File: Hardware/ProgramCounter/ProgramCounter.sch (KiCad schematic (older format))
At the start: 4 parts

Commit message: Started to make Schematic for the Program Counter.
TODO: Complete schematic, buy parts, layout PCB, solder PCB.

Then logically test the PCB using a digital oscilloscope.

Then repeat for 4-5 other PCBs.
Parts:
- removed UNOT: 74AUC1G04, symbol 74xGxx:74AUC1G04
- added C1, C2, C3, C4, C5, C6, C7: .1uF, symbol Device:C
- added U1: 74LS684, Package_SO:SSOP-20_3.9x8.7mm_P0.635mm, symbol 74xx_IEEE:74LS684
- added U2: 74151, Package_SO:SOP-16_4.55x10.3mm_P1.27mm, symbol 74xx_IEEE:74151
- added UNAND1: 74LS00, Package_SO:TSSOP-14_4.4x5mm_P0.65mm, symbol 74xx:74LS00
- added UQAND1: 74LS21, Package_SO:MSOP-12-16_3x4mm_P0.5mm, symbol 74xx:74LS21
- added UXOR1: 74HC86, Package_SO:SOIC-14_3.9x8.7mm_P1.27mm, symbol 74xx:74HC86
- J1: renamed from J?; footprint (none) -> Connector_PinSocket_2.54mm:PinSocket_2x32_P2.54mm_Horizontal
- UPR0, UPR1: footprint (none) -> Package_SO:SOIC-20W_7.5x12.8mm_P1.27mm
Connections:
- net labels added: IMM0, IMM1, IMM2, IMM3, IMM[0..3], IS_JMP, IS_SKIP, OPCODE[0..3], PCINC[0..15], PCOUT[0..15], RCD0, RCD1, RCD2, RCD3, RCD4, RCD5, RCD6, RCD7, RCD[0..3], RCS0, RCS1, RCS2, RCS3, RCS4, RCS5, RCS6, RCS7, RCS[0..3], REGMEM[0..15], cmpeq, cmpgt, cmplt
- net labels removed: OPCODE, PCINC, PCOUT, REGMEM
- wire segments 82 -> 183
- no-connect marks 1 -> 7
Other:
- note added: "Choose which condition to skip/jump on"
- moved on the sheet: UPR0, UPR1

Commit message: PC PCB Progress
Mostly done with schematic for the Program Counter. I'll order parts soon and start on the PCB design next. It'll be my first four layer board!

Based on what I've seen so far, CMOS seems to be more prevalent than TTL, so I'll make this computer out of CMOS.
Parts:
- removed J1: Conn_02x32_Row_Letter_First, Connector_PinSocket_2.54mm:PinSocket_2x32_P2.54mm_Horizontal, symbol Connector_Generic:Conn_02x32_Row_Letter_First
- added J1, J2: Conn_02x16_Counter_Clockwise, Connector_PinHeader_2.54mm:PinHeader_2x16_P2.54mm_Horizontal, symbol Connector_Generic:Conn_02x16_Counter_Clockwise
- added TP?: TP_PCEVENT, symbol Connector:TestPoint
- C1, C2, C3, C4, C5, C6, C7: footprint (none) -> Capacitor_SMD:C_1206_3216Metric_Pad1.42x1.75mm_HandSolder
- UQAND1: footprint Package_SO:MSOP-12-16_3x4mm_P0.5mm -> Package_SO:MSOP-12_3x4mm_P0.65mm
- renumbered U1 to UCMP1, U2 to UCONDMUX1
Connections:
- net labels added: JINST, PCEVENT, SINST, ~IS_JMP, ~IS_SKIP, ~OPCODE0, ~OPCODE1
- net labels removed: IS_JMP
- wire segments 183 -> 186
- no-connect marks 7 -> 4
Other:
- note added: "14ns"
- note added: "55ns"
- note added: "64ns"
- note added: "7ns"
- note added: "8ns"
- note added: "HC21 -> 22ns"
- note added: "HC86 -> 20ns"
- moved on the sheet: C1, C2, C3, C4, C5, C6, C7, UNAND1A, UNAND1B, UNAND1C, UNAND1D, UNAND1E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

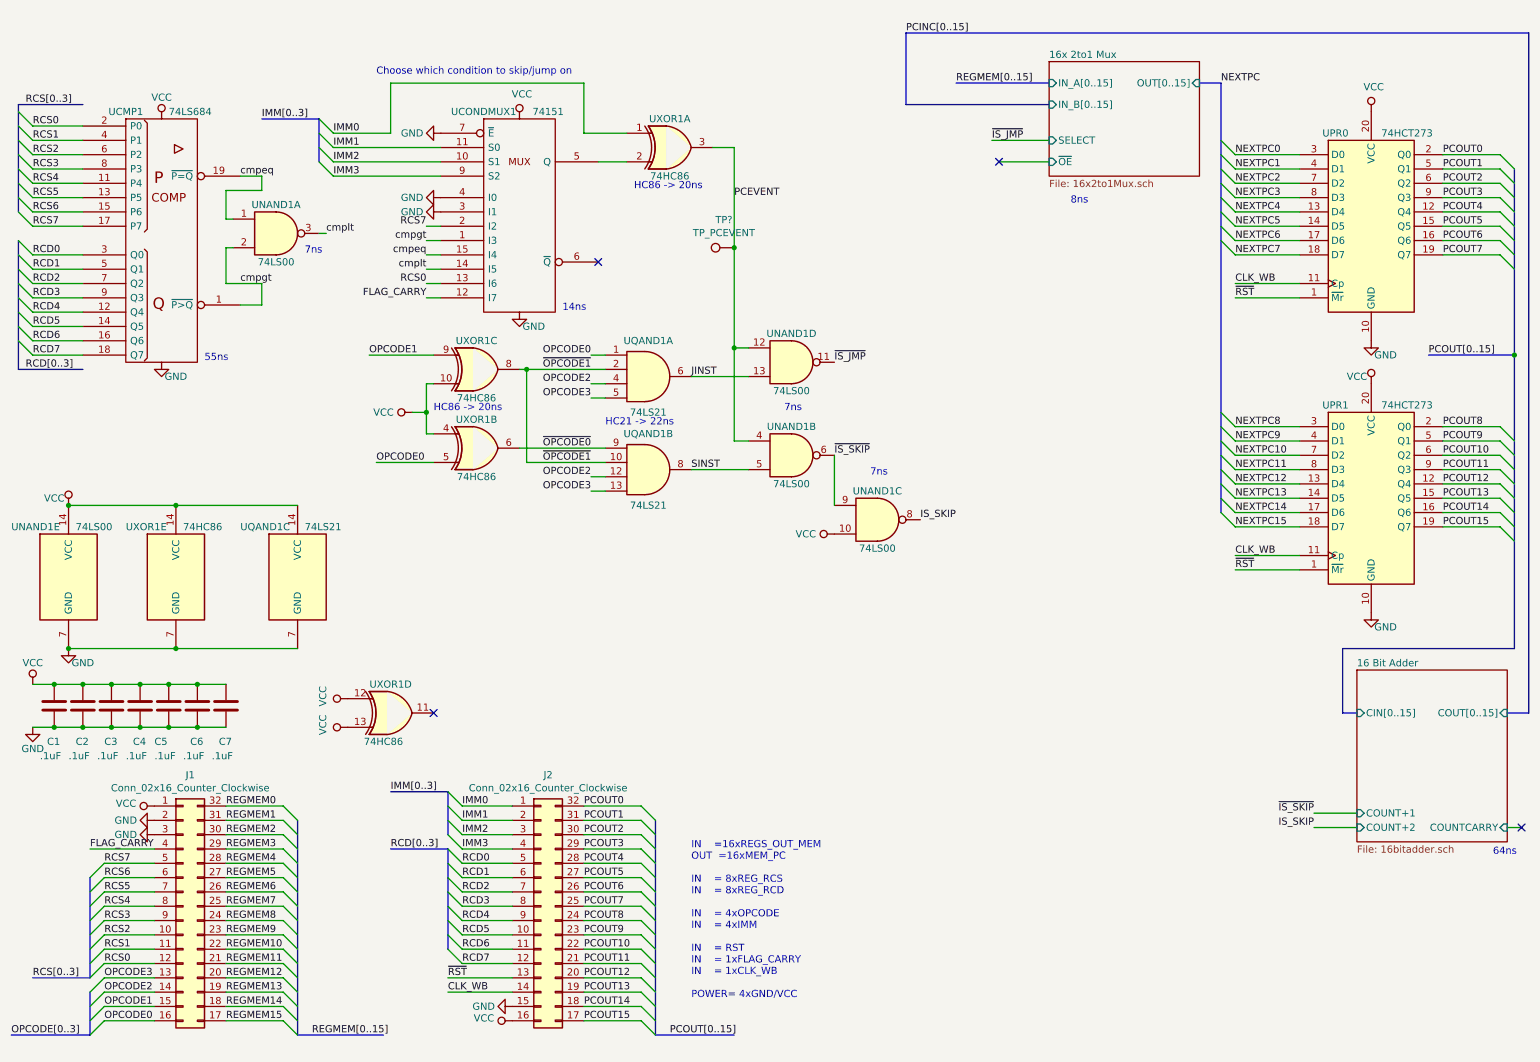
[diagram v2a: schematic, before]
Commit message: PC Schematic
Mostly finished Program Counter schematic. I'm basing the hardware largely off of TI's new HCS family of SN74HCS chips.
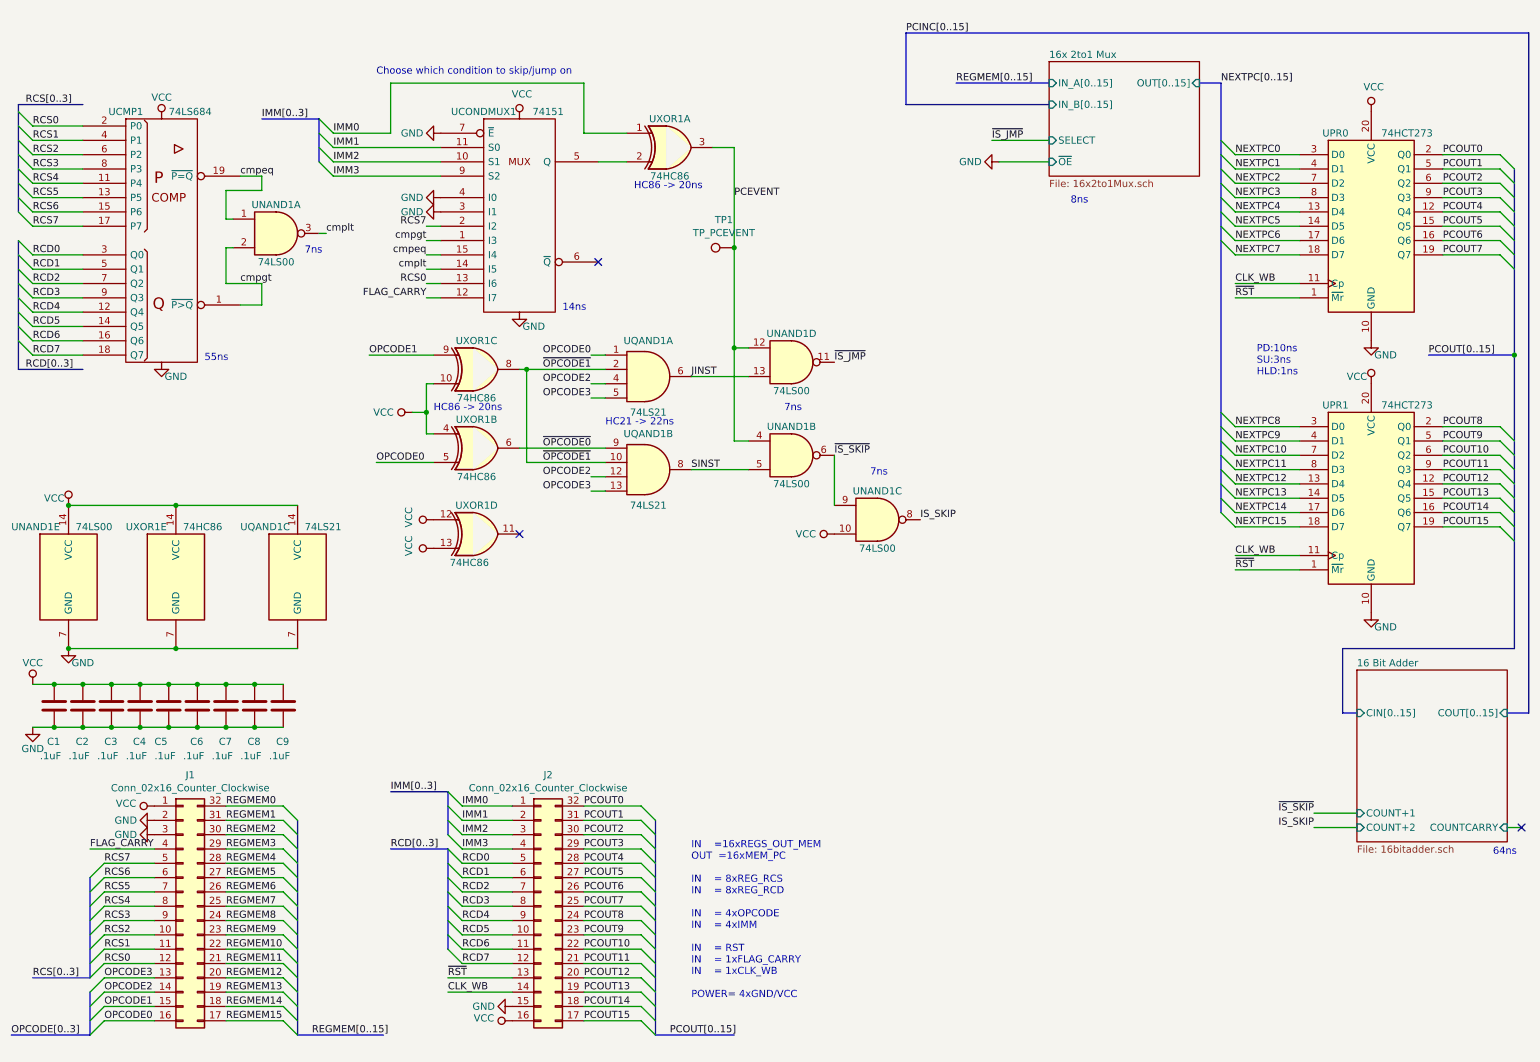
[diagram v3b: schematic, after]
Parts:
- added C8, C9: .1uF, Capacitor_SMD:C_1206_3216Metric_Pad1.42x1.75mm_HandSolder, symbol Device:C
- TP1: renamed from TP?; footprint (none) -> Connector_PinHeader_2.54mm:PinHeader_1x01_P2.54mm_Vertical
- UCMP1: footprint Package_SO:SSOP-20_3.9x8.7mm_P0.635mm -> aFootprint:DW0020A
- UCONDMUX1: footprint Package_SO:SOP-16_4.55x10.3mm_P1.27mm -> aFootprint:R-PDSO-G16
- UNAND1: footprint Package_SO:TSSOP-14_4.4x5mm_P0.65mm -> aFootprint:R-PDSO-G14
- UPR0, UPR1: footprint Package_SO:SOIC-20W_7.5x12.8mm_P1.27mm -> Package_SO:TSSOP-20_4.4x6.5mm_P0.65mm
- UQAND1: footprint Package_SO:MSOP-12_3x4mm_P0.65mm -> aFootprint:R-PDSO-G14
- UXOR1: footprint Package_SO:SOIC-14_3.9x8.7mm_P1.27mm -> aFootprint:R-PDSO-G14
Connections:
- net GND: now also C8.2, C9.2
- net VCC: now also C8.1, C9.1
- no-connect marks 4 -> 3
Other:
- note added: "PD:10ns\nSU:3ns\nHLD:1ns"
- moved on the sheet: UXOR1D
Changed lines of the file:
@@
 F 0 "UPR1" H 9750 4550 50  0000 C CNN
 F 1 "74HCT273" H 10250 4550 50  0000 C CNN
-F 2 "Package_SO:SOIC-20W_7.5x12.8mm_P1.27mm" H 10000 3900 50  0001 C CNN
+F 2 "Package_SO:TSSOP-20_4.4x6.5mm_P0.65mm" H 10000 3900 50  0001 C CNN
 F 3 "https://assets.nexperia.com/documents/data-sheet/74HC_HCT273.pdf" H 10000 3900 50  0001 C CNN
 	1    10000 3900
@@
 F 0 "UPR0" H 9750 2650 50  0000 C CNN
 F 1 "74HCT273" H 10250 2650 50  0000 C CNN
-F 2 "Package_SO:SOIC-20W_7.5x12.8mm_P1.27mm" H 10000 2000 50  0001 C CNN
+F 2 "Package_SO:TSSOP-20_4.4x6.5mm_P0.65mm" H 10000 2000 50  0001 C CNN
 F 3 "https://assets.nexperia.com/documents/data-sheet/74HC_HCT273.pdf" H 10000 2000 50  0001 C CNN
 	1    10000 2000
@@
 	8950 4000 9050 4100
 Text Label 8950 1000 0    50   ~ 0
-NEXTPC
+NEXTPC[0..15]
 Text Label 3550 7350 0    50   ~ 0
 CLK_WB
@@
 Wire Wire Line
 	7750 1550 7400 1550
-NoConn ~ 7400 1550
 Wire Bus Line
 	7100 1000 7750 1000
@@
 F 0 "UCMP1" H 1300 3000 50  0000 C CNN
 F 1 "74LS684" H 1750 3000 50  0000 C CNN
-F 2 "Package_SO:SSOP-20_3.9x8.7mm_P0.635mm" H 1550 2100 50  0001 C CNN
+F 2 "aFootprint:DW0020A" H 1550 2100 50  0001 C CNN
 F 3 "" H 1550 2100 50  0001 C CNN
 	1    1550 2100
@@
 F 0 "UNAND1" H 6550 4250 50  0000 C CNN
 F 1 "74LS00" H 6550 3850 50  0000 C CNN
-F 2 "Package_SO:TSSOP-14_4.4x5mm_P0.65mm" H 6550 4050 50  0001 C CNN
+F 2 "aFootprint:R-PDSO-G14" H 6550 4050 50  0001 C CNN
 F 3 "http://www.ti.com/lit/gpn/sn74ls00" H 6550 4050 50  0001 C CNN
 	3    6550 4050
@@
 F 0 "UNAND1" H 5950 3150 50  0000 C CNN
 F 1 "74LS00" H 5950 2750 50  0000 C CNN
-F 2 "Package_SO:TSSOP-14_4.4x5mm_P0.65mm" H 5950 2950 50  0001 C CNN
+F 2 "aFootprint:R-PDSO-G14" H 5950 2950 50  0001 C CNN
 F 3 "http://www.ti.com/lit/gpn/sn74ls00" H 5950 2950 50  0001 C CNN
 	4    5950 2950
@@
 F 0 "UNAND1" H 500 4800 50  0000 L CNN
 F 1 "74LS00" H 950 4800 50  0000 L CNN
-F 2 "Package_SO:TSSOP-14_4.4x5mm_P0.65mm" H 900 4450 50  0001 C CNN
+F 2 "aFootprint:R-PDSO-G14" H 900 4450 50  0001 C CNN
 F 3 "http://www.ti.com/lit/gpn/sn74ls00" H 900 4450 50  0001 C CNN
 	5    900  4450
@@
 F 0 "UCONDMUX1" H 3800 2600 50  0000 C CNN
 F 1 "74151" H 4250 2600 50  0000 C CNN
-F 2 "Package_SO:SOP-16_4.55x10.3mm_P1.27mm" H 4050 1900 50  0001 C CNN
+F 2 "aFootprint:R-PDSO-G16" H 4050 1900 50  0001 C CNN
 F 3 "" H 4050 1900 50  0001 C CNN
 	1    4050 1900
@@
 L 74xx:74HC86 UXOR1
 U 4 1 62FEDD88
-P 3150 5400
-F 0 "UXOR1" H 3150 5600 50  0000 C CNN
-F 1 "74HC86" H 3100 5200 50  0000 C CNN
-F 2 "Package_SO:SOIC-14_3.9x8.7mm_P1.27mm" H 3150 5400 50  0001 C CNN
-F 3 "http://www.ti.com/lit/gpn/sn74HC86" H 3150 5400 50  0001 C CNN
-	4    3150 5400
+P 3750 4150
+F 0 "UXOR1" H 3750 4350 50  0000 C CNN
+F 1 "74HC86" H 3700 3950 50  0000 C CNN
+F 2 "aFootprint:R-PDSO-G14" H 3750 4150 50  0001 C CNN
+F 3 "http://www.ti.com/lit/gpn/sn74HC86" H 3750 4150 50  0001 C CNN
+	4    3750 4150
 	1    0    0    -1
 $EndComp
@@
 F 0 "UXOR1" H 1300 4800 50  0000 L CNN
 F 1 "74HC86" H 1700 4800 50  0000 L CNN
-F 2 "Package_SO:SOIC-14_3.9x8.7mm_P1.27mm" H 1650 4450 50  0001 C CNN
+F 2 "aFootprint:R-PDSO-G14" H 1650 4450 50  0001 C CNN
 F 3 "http://www.ti.com/lit/gpn/sn74HC86" H 1650 4450 50  0001 C CNN
 	5    1650 4450
@@
 F 0 "UQAND1" H 4950 3950 50  0000 C CNN
 F 1 "74LS21" H 4950 3450 50  0000 C CNN
-F 2 "Package_SO:MSOP-12_3x4mm_P0.65mm" H 4950 3700 50  0001 C CNN
+F 2 "aFootprint:R-PDSO-G14" H 4950 3700 50  0001 C CNN
 F 3 "http://www.ti.com/lit/gpn/sn74LS21" H 4950 3700 50  0001 C CNN
 	2    4950 3700
@@
 F 0 "UXOR1" H 5100 1650 50  0000 C CNN
 F 1 "74HC86" H 5100 1250 50  0000 C CNN
-F 2 "Package_SO:SOIC-14_3.9x8.7mm_P1.27mm" H 5100 1450 50  0001 C CNN
+F 2 "aFootprint:R-PDSO-G14" H 5100 1450 50  0001 C CNN
 F 3 "http://www.ti.com/lit/gpn/sn74HC86" H 5100 1450 50  0001 C CNN
 	1    5100 1450
@@
 F 0 "UQAND1" H 4950 3300 50  0000 C CNN
 F 1 "74LS21" H 4950 2800 50  0000 C CNN
-F 2 "Package_SO:MSOP-12_3x4mm_P0.65mm" H 4950 3050 50  0001 C CNN
+F 2 "aFootprint:R-PDSO-G14" H 4950 3050 50  0001 C CNN
 F 3 "http://www.ti.com/lit/gpn/sn74LS21" H 4950 3050 50  0001 C CNN
 	1    4950 3050
@@
 F 0 "UNAND1" H 2350 2250 50  0000 C CNN
 F 1 "74LS00" H 2350 1850 50  0000 C CNN
-F 2 "Package_SO:TSSOP-14_4.4x5mm_P0.65mm" H 2350 2050 50  0001 C CNN
+F 2 "aFootprint:R-PDSO-G14" H 2350 2050 50  0001 C CNN
 F 3 "http://www.ti.com/lit/gpn/sn74ls00" H 2350 2050 50  0001 C CNN
 	1    2350 2050
@@
 F 0 "UNAND1" H 5950 3800 50  0000 C CNN
 F 1 "74LS00" H 5950 3400 50  0000 C CNN
-F 2 "Package_SO:TSSOP-14_4.4x5mm_P0.65mm" H 5950 3600 50  0001 C CNN
+F 2 "aFootprint:R-PDSO-G14" H 5950 3600 50  0001 C CNN
 F 3 "http://www.ti.com/lit/gpn/sn74ls00" H 5950 3600 50  0001 C CNN
 	2    5950 3600
@@
 	4050 3550 4650 3550
 $Comp
-L power:VCC #PWR?
+L power:VCC #PWR0109
 U 1 1 62FBF0AA
 P 3300 3300
-F 0 "#PWR?" H 3300 3150 50  0001 C CNN
+F 0 "#PWR0109" H 3300 3150 50  0001 C CNN
 F 1 "VCC" V 3300 3500 50  0000 C CNN
 F 2 "" H 3300 3300 50  0001 C CNN
@@
 F 0 "UQAND1" H 2100 4800 50  0000 L CNN
 F 1 "74LS21" H 2550 4800 50  0000 L CNN
-F 2 "Package_SO:MSOP-12_3x4mm_P0.65mm" H 2500 4450 50  0001 C CNN
+F 2 "aFootprint:R-PDSO-G14" H 2500 4450 50  0001 C CNN
 F 3 "http://www.ti.com/lit/gpn/sn74LS21" H 2500 4450 50  0001 C CNN
 	3    2500 4450
@@
 $EndComp
 $Comp
-L power:VCC #PWR?
+L power:VCC #PWR0110
 U 1 1 63082810
 P 650 5200
-F 0 "#PWR?" H 650 5050 50  0001 C CNN
+F 0 "#PWR0110" H 650 5050 50  0001 C CNN
 F 1 "VCC" H 650 5350 50  0000 C CNN
 F 2 "" H 650 5200 50  0001 C CNN
@@
 	650  5200 800  5200
 $Comp
-L power:GND #PWR?
+L power:GND #PWR0136
 U 1 1 63182DD6
 P 650 5500
-F 0 "#PWR?" H 650 5250 50  0001 C CNN
+F 0 "#PWR0136" H 650 5250 50  0001 C CNN
 F 1 "GND" H 650 5350 50  0000 C CNN
 F 2 "" H 650 5500 50  0001 C CNN
@@
 Connection ~ 5550 2850
 $Comp
-L power:VCC #PWR?
+L power:VCC #PWR0137
 U 1 1 6326BAED
-P 2850 5300
-F 0 "#PWR?" H 2850 5150 50  0001 C CNN
-F 1 "VCC" H 2867 5473 50  0000 C CNN
-F 2 "" H 2850 5300 50  0001 C CNN
-F 3 "" H 2850 5300 50  0001 C CNN
-	1    2850 5300
+P 3450 4050
+F 0 "#PWR0137" H 3450 3900 50  0001 C CNN
+F 1 "VCC" H 3467 4223 50  0000 C CNN
+F 2 "" H 3450 4050 50  0001 C CNN
+F 3 "" H 3450 4050 50  0001 C CNN
+	1    3450 4050
 	0    -1   -1   0
 $EndComp
 $Comp
-L power:VCC #PWR?
+L power:VCC #PWR0138
 U 1 1 6326C2DD
-P 2850 5500
-F 0 "#PWR?" H 2850 5350 50  0001 C CNN
-F 1 "VCC" H 2867 5673 50  0000 C CNN
-F 2 "" H 2850 5500 50  0001 C CNN
-F 3 "" H 2850 5500 50  0001 C CNN
-	1    2850 5500
+P 3450 4250
+F 0 "#PWR0138" H 3450 4100 50  0001 C CNN
+F 1 "VCC" H 3467 4423 50  0000 C CNN
+F 2 "" H 3450 4250 50  0001 C CNN
+F 3 "" H 3450 4250 50  0001 C CNN
+	1    3450 4250
 	0    -1   -1   0
 $EndComp
-NoConn ~ 3450 5400
+NoConn ~ 4050 4150
 Wire Wire Line
 	3450 3100 3400 3100
@@
 F 0 "UXOR1" H 3750 3200 50  0000 C CNN
 F 1 "74HC86" H 3750 2800 50  0000 C CNN
-F 2 "Package_SO:SOIC-14_3.9x8.7mm_P1.27mm" H 3750 3000 50  0001 C CNN
+F 2 "aFootprint:R-PDSO-G14" H 3750 3000 50  0001 C CNN
 F 3 "http://www.ti.com/lit/gpn/sn74HC86" H 3750 3000 50  0001 C CNN
 	3    3750 3000
@@
 ~IS_SKIP
 $Comp
-L Connector:TestPoint TP?
+L Connector:TestPoint TP1
 U 1 1 6337E135
 P 5550 2150
-F 0 "TP?" V 5745 2222 50  0000 C CNN
+F 0 "TP1" V 5745 2222 50  0000 C CNN
 F 1 "TP_PCEVENT" V 5654 2222 50  0000 C CNN
-F 2 "" H 5750 2150 50  0001 C CNN
+F 2 "Connector_PinHeader_2.54mm:PinHeader_1x01_P2.54mm_Vertical" H 5750 2150 50  0001 C CNN
 F 3 "~" H 5750 2150 50  0001 C CNN
 	1    5550 2150
@@
 F 0 "UXOR1" H 3750 3750 50  0000 C CNN
 F 1 "74HC86" H 3750 3350 50  0000 C CNN
-F 2 "Package_SO:SOIC-14_3.9x8.7mm_P1.27mm" H 3750 3550 50  0001 C CNN
+F 2 "aFootprint:R-PDSO-G14" H 3750 3550 50  0001 C CNN
 F 3 "http://www.ti.com/lit/gpn/sn74HC86" H 3750 3550 50  0001 C CNN
 	2    3750 3550
@@
 Wire Wire Line
 	9900 6100 9600 6100
+Text Notes 9200 3050 0    50   ~ 0
+PD:10ns\nSU:3ns\nHLD:1ns
+$Comp
+L power:GND #PWR0139
+U 1 1 62758916
+P 7400 1550
+F 0 "#PWR0139" H 7400 1300 50  0001 C CNN
+F 1 "GND" V 7400 1350 50  0000 C CNN
+F 2 "" H 7400 1550 50  0001 C CNN
+F 3 "" H 7400 1550 50  0001 C CNN
+	1    7400 1550
+	0    1    1    0
+$EndComp
+$Comp
+L Device:C C8
+U 1 1 627ABF70
+P 2200 5350
+F 0 "C8" H 2150 5100 50  0000 L CNN
+F 1 ".1uF" H 2100 5000 50  0000 L CNN
+F 2 "Capacitor_SMD:C_1206_3216Metric_Pad1.42x1.75mm_HandSolder" H 2238 5200 50  0001 C CNN
+F 3 "~" H 2200 5350 50  0001 C CNN
+	1    2200 5350
+	1    0    0    -1
+$EndComp
+$Comp
+L Device:C C9
+U 1 1 627ABF76
+P 2400 5350
+F 0 "C9" H 2350 5100 50  0000 L CNN
+F 1 ".1uF" H 2300 5000 50  0000 L CNN
+F 2 "Capacitor_SMD:C_1206_3216Metric_Pad1.42x1.75mm_HandSolder" H 2438 5200 50  0001 C CNN
+F 3 "~" H 2400 5350 50  0001 C CNN
+	1    2400 5350
+	1    0    0    -1
+$EndComp
+Wire Wire Line
+	2400 5500 2200 5500
+Connection ~ 2200 5200
+Wire Wire Line
+	2200 5200 2400 5200
+Connection ~ 2000 5200
+Wire Wire Line
+	2000 5200 2200 5200
+Wire Wire Line
+	2000 5500 2200 5500
+Connection ~ 2000 5500
+Connection ~ 2200 5500
 Wire Bus Line
 	3550 5950 3550 6250

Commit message: PC Board
Mostly done. Going to move top half down.
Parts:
- removed J1, J2: Conn_02x16_Counter_Clockwise, Connector_PinHeader_2.54mm:PinHeader_2x16_P2.54mm_Horizontal, symbol Connector_Generic:Conn_02x16_Counter_Clockwise
- added C? (x6): .1uF, Capacitor_SMD:C_1206_3216Metric_Pad1.42x1.75mm_HandSolder, symbol Device:C
- added J1, J2, J3, J4: Conn_02x08, Connector_PinSocket_2.54mm:PinSocket_2x08_P2.54mm_Horizontal, symbol Connector_Generic:Conn_02x08_Odd_Even
- UNAND1: value 74LS00 -> 74x00
- UPR0, UPR1: value 74HCT273 -> 74x273
- UQAND1: value 74LS21 -> 74x21
- UXOR1: value 74HC86 -> 74x86
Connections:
- net CLK_WB: now also J3.10 (Pin_10)
- net FLAG_CARRY: now also J3.5 (Pin_5)
- net GND: now also C?.2, C?.2, C?.2, C?.2, C?.2, C?.2, J3.1 (Pin_1), J3.15 (Pin_15), J3.16 (Pin_16)
- net IMM0: now also J3.13 (Pin_13)
- net IMM1: now also J3.11 (Pin_11)
- net IMM2: now also J3.9 (Pin_9)
- net IMM3: now also J3.7 (Pin_7)
- net OPCODE0: now also J3.2 (Pin_2)
- net OPCODE1: now also J3.4 (Pin_4)
- net OPCODE2: now also J3.6 (Pin_6)
- net OPCODE3: now also J3.8 (Pin_8)
- net PCOUT0: now also J4.1 (Pin_1)
- net PCOUT1: now also J4.2 (Pin_2)
- net PCOUT10: now also J4.11 (Pin_11)
- net PCOUT11: now also J4.12 (Pin_12)
- net PCOUT12: now also J4.13 (Pin_13)
- net PCOUT13: now also J4.14 (Pin_14)
- net PCOUT14: now also J4.15 (Pin_15)
- net PCOUT15: now also J4.16 (Pin_16)
- net PCOUT2: now also J4.3 (Pin_3)
- net PCOUT3: now also J4.4 (Pin_4)
- net PCOUT4: now also J4.5 (Pin_5)
- net PCOUT5: now also J4.6 (Pin_6)
- net PCOUT6: now also J4.7 (Pin_7)
- net PCOUT7: now also J4.8 (Pin_8)
- net PCOUT8: now also J4.9 (Pin_9)
- net PCOUT9: now also J4.10 (Pin_10)
- net RCD0: now also J2.15 (Pin_15)
- net RCD1: now also J2.13 (Pin_13)
- net RCD2: now also J2.11 (Pin_11)
- net RCD3: now also J2.9 (Pin_9)
- net RCD4: now also J2.7 (Pin_7)
- net RCD5: now also J2.5 (Pin_5)
- net RCD6: now also J2.3 (Pin_3)
- net RCD7: now also J2.1 (Pin_1)
- net RCS0: now also J2.16 (Pin_16)
- net RCS1: now also J2.14 (Pin_14)
- net RCS2: now also J2.12 (Pin_12)
- net RCS3: now also J2.10 (Pin_10)
- net RCS4: now also J2.8 (Pin_8)
- net RCS5: now also J2.6 (Pin_6)
- net RCS6: now also J2.4 (Pin_4)
- net RCS7: now also J2.2 (Pin_2)
- net REGMEM0: now also J1.1 (Pin_1)
- net REGMEM1: now also J1.2 (Pin_2)
- net REGMEM10: now also J1.11 (Pin_11)
- net REGMEM11: now also J1.12 (Pin_12)
- net REGMEM12: now also J1.13 (Pin_13)
- net REGMEM13: now also J1.14 (Pin_14)
- net REGMEM14: now also J1.15 (Pin_15)
- net REGMEM15: now also J1.16 (Pin_16)
- net REGMEM2: now also J1.3 (Pin_3)
- net REGMEM3: now also J1.4 (Pin_4)
- net REGMEM4: now also J1.5 (Pin_5)
- net REGMEM5: now also J1.8 (Pin_8)
- net REGMEM6: now also J1.7 (Pin_7)
- net REGMEM7: now also J1.6 (Pin_6)
- net REGMEM8: now also J1.9 (Pin_9)
- net REGMEM9: now also J1.10 (Pin_10)
- net VCC: now also C?.1, C?.1, C?.1, C?.1, C?.1, C?.1, J3.14 (Pin_14), J3.3 (Pin_3)
- net ~RST: now also J3.12 (Pin_12)
